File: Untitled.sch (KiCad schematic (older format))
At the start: 7 parts

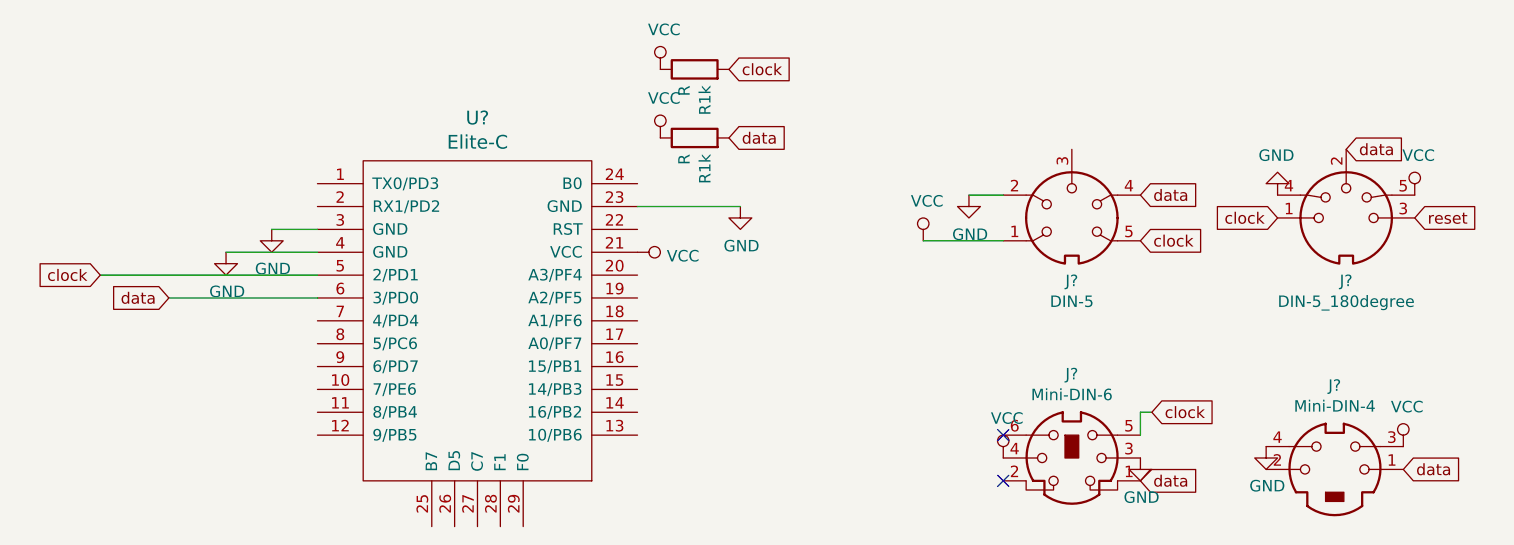
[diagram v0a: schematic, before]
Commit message: Made PCB.
Still need to add 240º DIN connector.
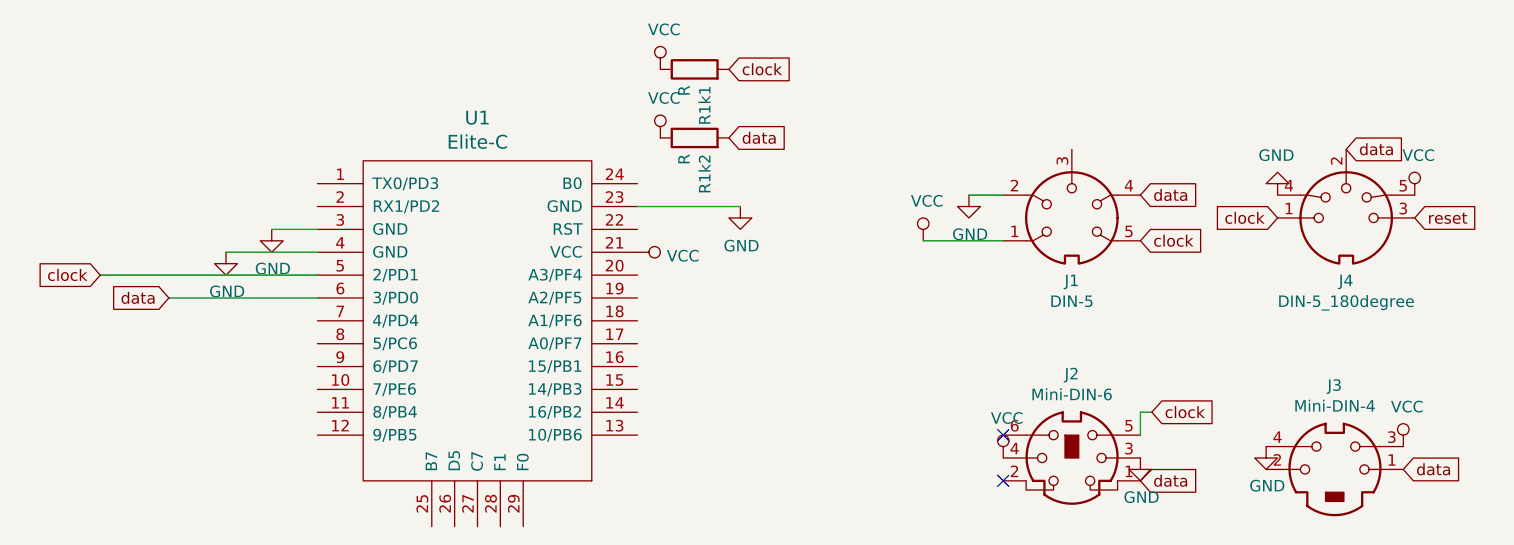
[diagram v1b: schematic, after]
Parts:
- J2: renamed from J?; footprint (none) -> KMDGX-6S-BS:KMDGX6SBS
- J3: renamed from J?; footprint (none) -> MD-40SM:MD40SM
- J4: renamed from J?; footprint (none) -> 57PC5F:57PC5F
- R1k1, R1k2: renamed from R1k; footprint (none) -> Keebio-Parts:Resistor
- U1: renamed from U?; footprint (none) -> Keebio-Parts:Elite-C-ZigZag
- gave numbers to parts that had none: 1
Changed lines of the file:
@@
 $EndDescr
 $Comp
-L keebio:Elite-C U?
+L keebio:Elite-C U1
 U 1 1 5D915DFE
 P 4550 2000
-F 0 "U?" H 4550 2837 60  0000 C CNN
+F 0 "U1" H 4550 2837 60  0000 C CNN
 F 1 "Elite-C" H 4550 2731 60  0000 C CNN
-F 2 "" V 5600 -500 60  0001 C CNN
+F 2 "Keebio-Parts:Elite-C-ZigZag" V 5600 -500 60  0001 C CNN
 F 3 "" V 5600 -500 60  0001 C CNN
 	1    4550 2000
@@
 $EndComp
 $Comp
-L Connector:DIN-5 J?
+L Connector:DIN-5 J1
 U 1 1 5D916F72
 P 7150 1600
-F 0 "J?" H 7150 1325 50  0000 C CNN
+F 0 "J1" H 7150 1325 50  0000 C CNN
 F 1 "DIN-5" H 7150 1234 50  0000 C CNN
 F 2 "" H 7150 1600 50  0001 C CNN
@@
 $EndComp
 $Comp
-L Connector:DIN-5_180degree J?
+L Connector:DIN-5_180degree J4
 U 1 1 5D917CAD
 P 8350 1600
-F 0 "J?" H 8350 1325 50  0000 C CNN
+F 0 "J4" H 8350 1325 50  0000 C CNN
 F 1 "DIN-5_180degree" H 8350 1234 50  0000 C CNN
-F 2 "" H 8350 1600 50  0001 C CNN
+F 2 "57PC5F:57PC5F" H 8350 1600 50  0001 C CNN
 F 3 "http://www.mouser.com/ds/2/18/40_c091_abd_e-75918.pdf" H 8350 1600 50  0001 C CNN
 	1    8350 1600
@@
 $EndComp
 $Comp
-L Connector:Mini-DIN-6 J?
+L Connector:Mini-DIN-6 J2
 U 1 1 5D919651
 P 7150 2650
-F 0 "J?" H 7150 3017 50  0000 C CNN
+F 0 "J2" H 7150 3017 50  0000 C CNN
 F 1 "Mini-DIN-6" H 7150 2926 50  0000 C CNN
-F 2 "" H 7150 2650 50  0001 C CNN
+F 2 "KMDGX-6S-BS:KMDGX6SBS" H 7150 2650 50  0001 C CNN
 F 3 "http://service.powerdynamics.com/ec/Catalog17/Section%2011.pdf" H 7150 2650 50  0001 C CNN
 	1    7150 2650
@@
 $EndComp
 $Comp
-L Connector:Mini-DIN-4 J?
+L Connector:Mini-DIN-4 J3
 U 1 1 5D91AA06
 P 8300 2700
-F 0 "J?" H 8300 3067 50  0000 C CNN
+F 0 "J3" H 8300 3067 50  0000 C CNN
 F 1 "Mini-DIN-4" H 8300 2976 50  0000 C CNN
-F 2 "" H 8300 2700 50  0001 C CNN
+F 2 "MD-40SM:MD40SM" H 8300 2700 50  0001 C CNN
 F 3 "http://service.powerdynamics.com/ec/Catalog17/Section%2011.pdf" H 8300 2700 50  0001 C CNN
 	1    8300 2700
@@
 $EndComp
 $Comp
-L Device:R R1k
+L Device:R R1k1
 U 1 1 5D91B2DE
 P 5500 950
-F 0 "R1k" H 5430 904 50  0000 R CNN
+F 0 "R1k1" H 5430 904 50  0000 R CNN
 F 1 "R" H 5430 995 50  0000 R CNN
-F 2 "" V 5430 950 50  0001 C CNN
+F 2 "Keebio-Parts:Resistor" V 5430 950 50  0001 C CNN
 F 3 "~" H 5500 950 50  0001 C CNN
 	1    5500 950
@@
 $EndComp
 $Comp
-L Device:R R1k
+L Device:R R1k2
 U 1 1 5D910C81
 P 5500 1250
-F 0 "R1k" H 5430 1204 50  0000 R CNN
+F 0 "R1k2" H 5430 1204 50  0000 R CNN
 F 1 "R" H 5430 1295 50  0000 R CNN
-F 2 "" V 5430 1250 50  0001 C CNN
+F 2 "Keebio-Parts:Resistor" V 5430 1250 50  0001 C CNN
 F 3 "~" H 5500 1250 50  0001 C CNN
 	1    5500 1250
@@
 $EndComp
 $Comp
-L power:VCC #PWR?
+L power:VCC #PWR0101
 U 1 1 5D9144E6
 P 6500 1700
-F 0 "#PWR?" H 6500 1550 50  0001 C CNN
+F 0 "#PWR0101" H 6500 1550 50  0001 C CNN
 F 1 "VCC" H 6517 1873 50  0000 C CNN
 F 2 "" H 6500 1700 50  0001 C CNN
@@
 $EndComp
 $Comp
-L power:VCC #PWR?
+L power:VCC #PWR0102
 U 1 1 5D914B74
 P 8600 2600
-F 0 "#PWR?" H 8600 2450 50  0001 C CNN
+F 0 "#PWR0102" H 8600 2450 50  0001 C CNN
 F 1 "VCC" H 8617 2773 50  0000 C CNN
 F 2 "" H 8600 2600 50  0001 C CNN
@@
 $EndComp
 $Comp
-L power:VCC #PWR?
+L power:VCC #PWR0103
 U 1 1 5D91690F
 P 6850 2650
-F 0 "#PWR?" H 6850 2500 50  0001 C CNN
+F 0 "#PWR0103" H 6850 2500 50  0001 C CNN
 F 1 "VCC" H 6867 2823 50  0000 C CNN
 F 2 "" H 6850 2650 50  0001 C CNN
@@
 data
 $Comp
-L power:GND #PWR?
+L power:GND #PWR0104
 U 1 1 5D9182F9
 P 7450 2650
-F 0 "#PWR?" H 7450 2400 50  0001 C CNN
+F 0 "#PWR0104" H 7450 2400 50  0001 C CNN
 F 1 "GND" H 7455 2477 50  0000 C CNN
 F 2 "" H 7450 2650 50  0001 C CNN
@@
 $EndComp
 $Comp
-L power:GND #PWR?
+L power:GND #PWR0105
 U 1 1 5D91851B
 P 8000 2600
-F 0 "#PWR?" H 8000 2350 50  0001 C CNN
+F 0 "#PWR0105" H 8000 2350 50  0001 C CNN
 F 1 "GND" H 8005 2427 50  0000 C CNN
 F 2 "" H 8000 2600 50  0001 C CNN
@@
 $EndComp
 $Comp
-L power:GND #PWR?
+L power:GND #PWR0106
 U 1 1 5D919A75
 P 6700 1500
-F 0 "#PWR?" H 6700 1250 50  0001 C CNN
+F 0 "#PWR0106" H 6700 1250 50  0001 C CNN
 F 1 "GND" H 6705 1327 50  0000 C CNN
 F 2 "" H 6700 1500 50  0001 C CNN
@@
 	6850 1500 6700 1500
 $Comp
-L power:VCC #PWR?
+L power:VCC #PWR0107
 U 1 1 5D91A6F9
 P 5350 1250
-F 0 "#PWR?" H 5350 1100 50  0001 C CNN
+F 0 "#PWR0107" H 5350 1100 50  0001 C CNN
 F 1 "VCC" H 5367 1423 50  0000 C CNN
 F 2 "" H 5350 1250 50  0001 C CNN
@@
 $EndComp
 $Comp
-L power:VCC #PWR?
+L power:VCC #PWR0108
 U 1 1 5D91A9A0
 P 5350 950
-F 0 "#PWR?" H 5350 800 50  0001 C CNN
+F 0 "#PWR0108" H 5350 800 50  0001 C CNN
 F 1 "VCC" H 5367 1123 50  0000 C CNN
 F 2 "" H 5350 950 50  0001 C CNN
@@
 clock
 $Comp
-L power:GND #PWR?
+L power:GND #PWR0109
 U 1 1 5D91BF4C
 P 8050 1500
-F 0 "#PWR?" H 8050 1250 50  0001 C CNN
+F 0 "#PWR0109" H 8050 1250 50  0001 C CNN
 F 1 "GND" H 8055 1327 50  0000 C CNN
 F 2 "" H 8050 1500 50  0001 C CNN
@@
 data
 $Comp
-L power:VCC #PWR?
+L power:VCC #PWR0110
 U 1 1 5D91C566
 P 8650 1500
-F 0 "#PWR?" H 8650 1350 50  0001 C CNN
+F 0 "#PWR0110" H 8650 1350 50  0001 C CNN
 F 1 "VCC" H 8667 1673 50  0000 C CNN
 F 2 "" H 8650 1500 50  0001 C CNN
@@
 clock
 $Comp
-L power:GND #PWR?
+L power:GND #PWR0111
 U 1 1 5D92272B
 P 3650 1650
-F 0 "#PWR?" H 3650 1400 50  0001 C CNN
+F 0 "#PWR0111" H 3650 1400 50  0001 C CNN
 F 1 "GND" H 3655 1477 50  0000 C CNN
 F 2 "" H 3650 1650 50  0001 C CNN
@@
 $EndComp
 $Comp
-L power:GND #PWR?
+L power:GND #PWR0112
 U 1 1 5D92296F
 P 3450 1750
-F 0 "#PWR?" H 3450 1500 50  0001 C CNN
+F 0 "#PWR0112" H 3450 1500 50  0001 C CNN
 F 1 "GND" H 3455 1577 50  0000 C CNN
 F 2 "" H 3450 1750 50  0001 C CNN
@@
 $EndComp
 $Comp
-L power:VCC #PWR?
+L power:VCC #PWR0113
 U 1 1 5D923369
 P 5250 1750
-F 0 "#PWR?" H 5250 1600 50  0001 C CNN
+F 0 "#PWR0113" H 5250 1600 50  0001 C CNN
 F 1 "VCC" V 5267 1878 50  0000 L CNN
 F 2 "" H 5250 1750 50  0001 C CNN
@@
 $EndComp
 $Comp
-L power:GND #PWR?
+L power:GND #PWR0114
 U 1 1 5D924B01
 P 5700 1550
-F 0 "#PWR?" H 5700 1300 50  0001 C CNN
+F 0 "#PWR0114" H 5700 1300 50  0001 C CNN
 F 1 "GND" H 5705 1377 50  0000 C CNN
 F 2 "" H 5700 1550 50  0001 C CNN
